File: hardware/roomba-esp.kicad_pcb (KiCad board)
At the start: 2 copper layers, 45 x 32.5 mm, 7 parts, among them P1 CONN_01X07, P2 CONN_02X10, U1 ESP-12E, U2 LM2596_module

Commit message: finalised rev0 pcb
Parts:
- P1: footprint mini din:mini din 7 -> mini din:mini_DIN_7
- moved U2 20.9 mm to (192.0, 118.0), turned to 0 degrees
- moved R1 13.4 mm to (181.0, 111.0), turned to 90 degrees
- moved D1 12.5 mm to (181.0, 116.0)
- moved R2 12.4 mm to (181.0, 121.0)
- moved P2 9.03 mm to (205.7, 127.0)
- moved P1 7.85 mm to (214.0, 98.5), turned to 90 degrees
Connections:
- P2 pad 10: /SCK -> /MISO
- P2 pad 12: /MOSI -> /CS0
- P2 pad 14: /MISO -> /GPIO16
- P2 pad 16: /CS0 -> /GPIO15
- P2 pad 18: /GPIO16 -> /GPIO14
- P2 pad 19: /GPIO14 -> /ADC
- P2 pad 20: /GPIO15 -> /RESET
- P2 pad 6: /ADC -> /SCK
- P2 pad 8: /RESET -> /MOSI
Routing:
- net /GPIO15: track 0.00 -> 52.3 mm, vias 0 -> 1
- net /RESET: track 0.00 -> 40.8 mm
- net /ADC: track 0.00 -> 36.4 mm
- net /GPIO13: track 16.2 -> 40.6 mm, vias 0 -> 1
- net /TX: track 0.00 -> 16.0 mm
- net /GPIO10: track 14.3 -> 29.6 mm, vias 1 -> 0
- net /SCK: track 15.3 -> 0.00 mm
- net /GPIO16: track 31.8 -> 44.0 mm
- net /GPIO14: track 21.5 -> 33.7 mm, vias 0 -> 1
- net /GPIO12: track 19.5 -> 28.5 mm, vias 0 -> 1
- net Net-(R1-Pad2): track 7.40 -> 15.8 mm
- net /MISO: track 14.0 -> 22.4 mm
- net /CS0: track 14.3 -> 22.2 mm
- net /RX: track 0.00 -> 7.36 mm
- net /DD: track 0.00 -> 7.20 mm
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- added copper zone on F.Cu, net GND
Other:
- board size 45 x 32.5 mm -> 33 x 40 mm
- net class Power: clearance 0.3 -> 0.25

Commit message: fixed some kicad-level path/library setings
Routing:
- net GND: track 4.62 -> 106.4 mm, vias 0 -> 1
- net VCC: track 7.48 -> 37.8 mm
- net /VBat: track 68.9 -> 39.5 mm
- net /SCK: track 0.00 -> 20.8 mm
- net /RESET: track 40.8 -> 45.1 mm, vias 0 -> 1
- net /GPIO0: track 30.2 -> 28.6 mm
- net /GPIO2: track 29.7 -> 29.9 mm, vias 0 -> 1
- added copper zone on B.Cu, net GND

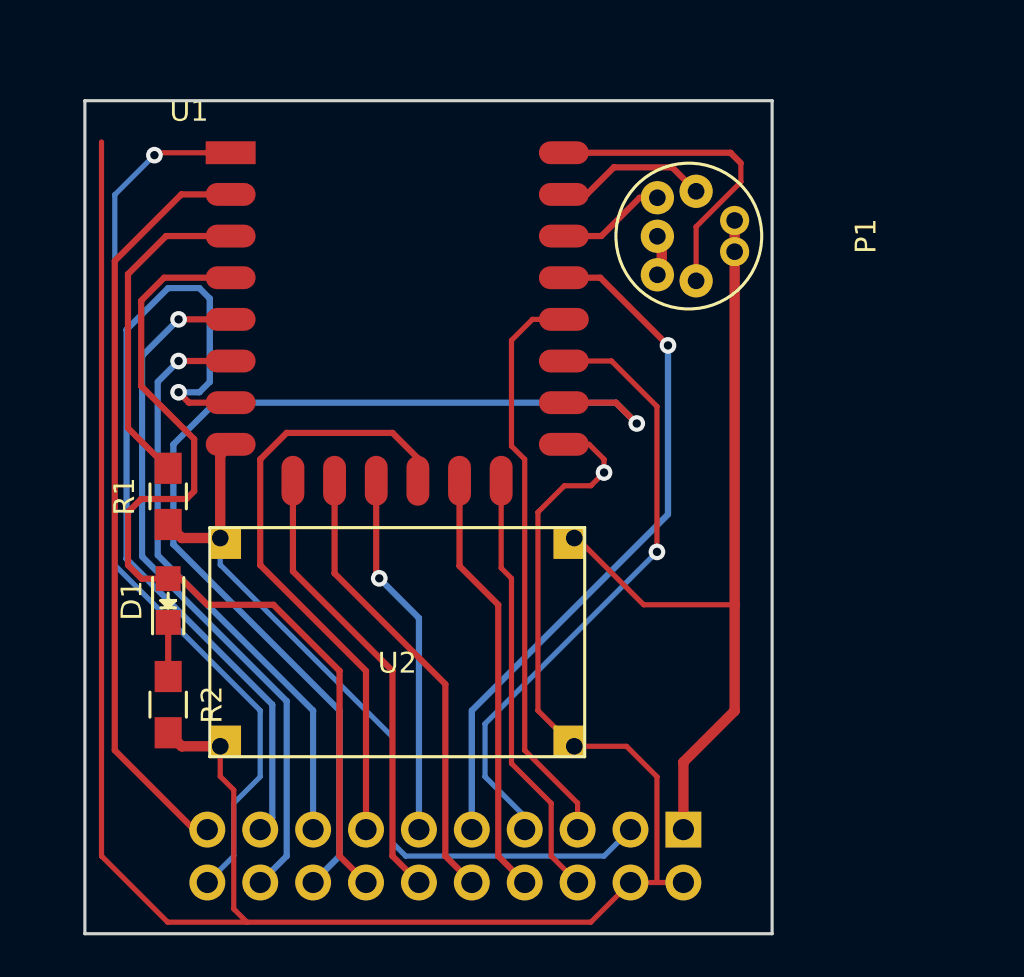
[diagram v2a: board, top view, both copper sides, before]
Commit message: added voltage divider on ESP RX to accomodate for 5V level on 3.3V pin
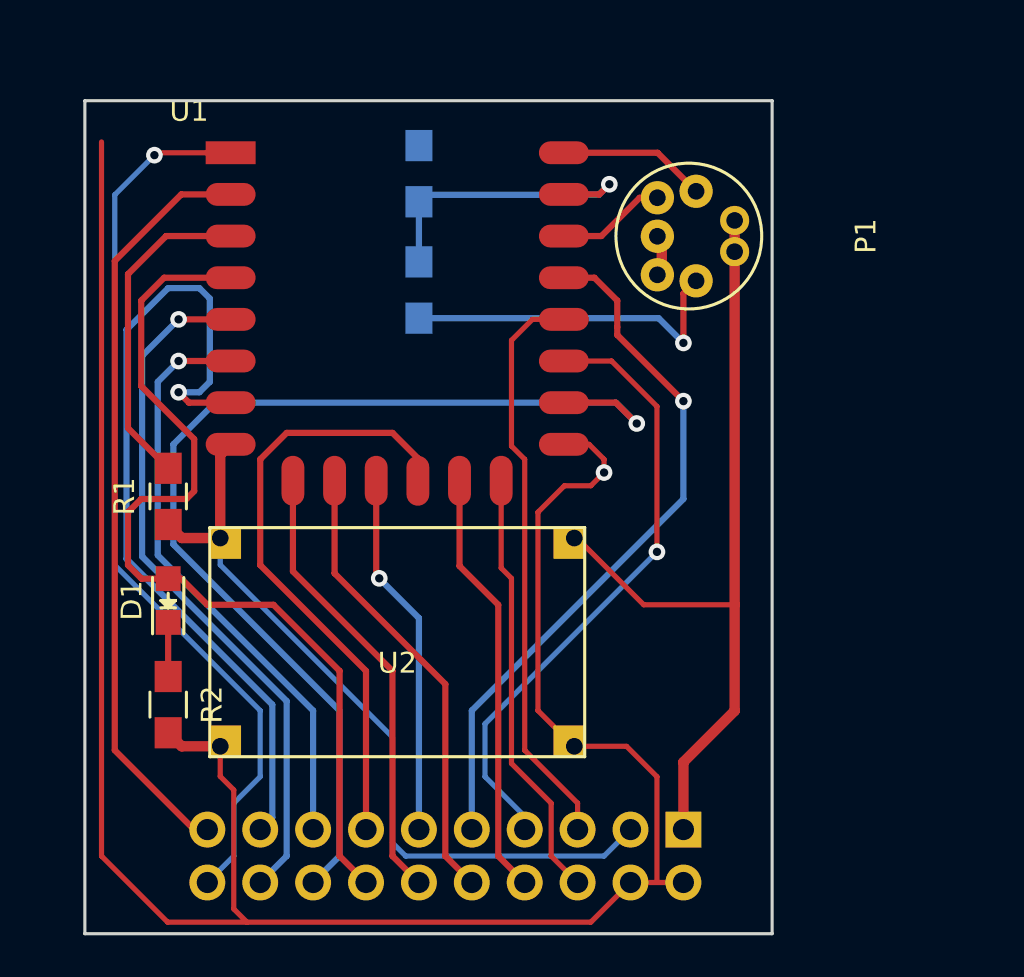
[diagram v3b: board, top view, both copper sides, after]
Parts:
- added R3: R, Resistors_SMD:R_0805_HandSoldering, B.Cu at (193.0, 101.1)
- added R4: R, Resistors_SMD:R_0805_HandSoldering, B.Cu at (193.0, 95.5)
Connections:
- P1 pad 3: /RX -> /RX_R
- P1 pad 4: /TX -> /TX_R
- U1 pad 22: /TX -> /RX_R
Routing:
- net /TX_R: track 0.00 -> 16.4 mm, vias 0 -> 1
- net /TX: track 16.0 -> 0.00 mm
- net /RX: track 7.36 -> 16.3 mm, vias 0 -> 1
- net /RX_R: track 0.00 -> 7.92 mm
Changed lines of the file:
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@@
-(kicad_pcb (version 4) (host pcbnew "(2015-09-21 BZR 6208, Git 1d27d08)-product")
+(kicad_pcb (version 4) (host pcbnew 0.201509251831+6217~30~ubuntu15.04.1-product)
   (general
-    (links 35)
+    (links 38)
     (no_connects 0)
-    (area 176.924999 91.924999 210.075001 132.075001)
+    (area 165.000001 85.773799 215.525 136.700001)
     (thickness 1.6)
     (drawings 6)
-    (tracks 192)
+    (tracks 202)
     (zones 0)
-    (modules 7)
-    (nets 25)
+    (modules 9)
+    (nets 26)
   )
   (page A4)
@@
     (31 B.Cu signal)
     (32 B.Adhes user)
-    (33 F.Adhes user)
+    (33 F.Adhes user hide)
     (34 B.Paste user)
     (35 F.Paste user)
@@
   )
   (setup
-    (last_trace_width 0.25)
+    (last_trace_width 0.3)
     (user_trace_width 0.25)
     (trace_clearance 0.25)
@@
   (net 22 /DD)
   (net 23 /RX)
-  (net 24 /TX)
+  (net 24 /TX_R)
+  (net 25 /RX_R)
   (net_class Default "This is the default net class."
     (clearance 0.25)
@@
     (add_net /RESET)
     (add_net /RX)
+    (add_net /RX_R)
     (add_net /SCK)
-    (add_net /TX)
+    (add_net /TX_R)
     (add_net "Net-(D1-Pad1)")
     (add_net "Net-(R1-Pad2)")
@@
       (net 23 /RX))
     (pad 22 smd oval (at 16 0) (size 2.4 1.1) (layers F.Cu F.Paste F.Mask)
-      (net 24 /TX))
+      (net 25 /RX_R))
   )
   (module Socket_Strips:Socket_Strip_Straight_2x10 (layer B.Cu)
@@
       (net 22 /DD))
     (pad 4 thru_hole circle (at -2.15 -7.65 90) (size 1.6 1.6) (drill 0.8) (layers *.Cu *.Mask F.SilkS)
-      (net 24 /TX))
+      (net 24 /TX_R))
     (pad 3 thru_hole circle (at 2.15 -7.65 90) (size 1.6 1.6) (drill 0.8) (layers *.Cu *.Mask F.SilkS)
-      (net 23 /RX))
+      (net 25 /RX_R))
     (pad 1 thru_hole circle (at 0.75 -5.8 90) (size 1.4 1.4) (drill 0.8) (layers *.Cu *.Mask F.SilkS)
       (net 3 /VBat))
     (pad 2 thru_hole circle (at -0.75 -5.8 90) (size 1.4 1.4) (drill 0.8) (layers *.Cu *.Mask F.SilkS)
       (net 3 /VBat))
+  )
+  (module Resistors_SMD:R_0805_HandSoldering (layer B.Cu)
+    (at 193.04 101.092 90)
+    (descr "Resistor SMD 0805, hand soldering")
+    (tags "resistor 0805")
+    (attr smd)
+    (fp_text reference R3 (at 0 2.1 90) (layer B.SilkS)
+      (effects (font (size 1 1) (thickness 0.15)) (justify mirror))
+    )
+    (fp_text value R (at 0 -2.1 90) (layer B.Fab)
+      (effects (font (size 1 1) (thickness 0.15)) (justify mirror))
+    )
+    (fp_line (start -2.4 1) (end 2.4 1) (layer B.CrtYd) (width 0.05))
+    (fp_line (start -2.4 -1) (end 2.4 -1) (layer B.CrtYd) (width 0.05))
+    (fp_line (start -2.4 1) (end -2.4 -1) (layer B.CrtYd) (width 0.05))
+    (fp_line (start 2.4 1) (end 2.4 -1) (layer B.CrtYd) (width 0.05))
+    (fp_line (start 0.6 -0.875) (end -0.6 -0.875) (layer B.SilkS) (width 0.15))
+    (fp_line (start -0.6 0.875) (end 0.6 0.875) (layer B.SilkS) (width 0.15))
+    (pad 1 smd rect (at -1.35 0 90) (size 1.5 1.3) (layers B.Cu B.Paste B.Mask)
+      (net 24 /TX_R))
+    (pad 2 smd rect (at 1.35 0 90) (size 1.5 1.3) (layers B.Cu B.Paste B.Mask)
+      (net 23 /RX))
+    (model Resistors_SMD.3dshapes/R_0805_HandSoldering.wrl
+      (at (xyz 0 0 0))
+      (scale (xyz 1 1 1))
+      (rotate (xyz 0 0 0))
+    )
+  )
+  (module Resistors_SMD:R_0805_HandSoldering (layer B.Cu)
+    (at 193.04 95.504 90)
+    (descr "Resistor SMD 0805, hand soldering")
+    (tags "resistor 0805")
+    (attr smd)
+    (fp_text reference R4 (at 0 2.1 90) (layer B.SilkS)
+      (effects (font (size 1 1) (thickness 0.15)) (justify mirror))
+    )
+    (fp_text value R (at 0 -2.1 90) (layer B.Fab)
+      (effects (font (size 1 1) (thickness 0.15)) (justify mirror))
+    )
+    (fp_line (start -2.4 1) (end 2.4 1) (layer B.CrtYd) (width 0.05))
+    (fp_line (start -2.4 -1) (end 2.4 -1) (layer B.CrtYd) (width 0.05))
+    (fp_line (start -2.4 1) (end -2.4 -1) (layer B.CrtYd) (width 0.05))
+    (fp_line (start 2.4 1) (end 2.4 -1) (layer B.CrtYd) (width 0.05))
+    (fp_line (start 0.6 -0.875) (end -0.6 -0.875) (layer B.SilkS) (width 0.15))
+    (fp_line (start -0.6 0.875) (end 0.6 0.875) (layer B.SilkS) (width 0.15))
+    (pad 1 smd rect (at -1.35 0 90) (size 1.5 1.3) (layers B.Cu B.Paste B.Mask)
+      (net 23 /RX))
+    (pad 2 smd rect (at 1.35 0 90) (size 1.5 1.3) (layers B.Cu B.Paste B.Mask)
+      (net 4 GND))
+    (model Resistors_SMD.3dshapes/R_0805_HandSoldering.wrl
+      (at (xyz 0 0 0))
+      (scale (xyz 1 1 1))
+      (rotate (xyz 0 0 0))
+    )
   )
   (dimension 40 (width 0.3) (layer Cmts.User)
@@
   (segment (start 182.88 129.54) (end 182.245 129.54) (width 0.3) (layer F.Cu) (net 9) (status 30))
   (segment (start 182.85218 94.5) (end 184 94.5) (width 0.3) (layer F.Cu) (net 9) (status 30))
-  (segment (start 195.58 127) (end 195.58 121.285) (width 0.3) (layer B.Cu) (net 10) (status 10))
-  (segment (start 201.75 100.5) (end 200 100.5) (width 0.3) (layer F.Cu) (net 10) (status 20))
-  (segment (start 205 103.75) (end 201.75 100.5) (width 0.3) (layer F.Cu) (net 10))
-  (via (at 205 103.75) (size 0.8) (drill 0.4) (layers F.Cu B.Cu) (net 10))
-  (segment (start 205 111.865) (end 205 103.75) (width 0.3) (layer B.Cu) (net 10))
-  (segment (start 195.58 121.285) (end 205 111.865) (width 0.3) (layer B.Cu) (net 10))
+  (segment (start 205.74 111.125) (end 205.74 106.426) (width 0.3) (layer B.Cu) (net 10))
+  (segment (start 201.465 100.5) (end 202.565 101.6) (width 0.3) (layer F.Cu) (net 10))
+  (segment (start 202.565 101.6) (end 202.565 102.87) (width 0.3) (layer F.Cu) (net 10))
+  (segment (start 195.58 121.285) (end 205.74 111.125) (width 0.3) (layer B.Cu) (net 10))
+  (segment (start 195.58 127) (end 195.58 121.285) (width 0.3) (layer B.Cu) (net 10))
+  (segment (start 201.465 100.5) (end 200 100.5) (width 0.3) (layer F.Cu) (net 10))
+  (segment (start 202.565 103.251) (end 202.565 102.87) (width 0.3) (layer F.Cu) (net 10))
+  (segment (start 205.74 106.426) (end 202.565 103.251) (width 0.3) (layer F.Cu) (net 10))
+  (via (at 205.74 106.426) (size 0.8) (drill 0.4) (layers F.Cu B.Cu) (net 10))
   (segment (start 200.66 129.54) (end 199.39 128.27) (width 0.25) (layer F.Cu) (net 11) (status 10))
   (segment (start 196.99 114.44) (end 196.99 110.25) (width 0.25) (layer F.Cu) (net 11) (status 20))
@@
   (segment (start 199.39 125.73) (end 197.485 123.825) (width 0.25) (layer F.Cu) (net 11))
   (segment (start 199.39 128.27) (end 199.39 125.73) (width 0.25) (layer F.Cu) (net 11))
+  (via (at 191.135 114.935) (size 0.8) (drill 0.4) (layers F.Cu B.Cu) (net 12))
   (segment (start 193.04 127) (end 193.04 116.84) (width 0.3) (layer B.Cu) (net 12) (status 10))
+  (segment (start 193.04 116.84) (end 191.135 114.935) (width 0.3) (layer B.Cu) (net 12))
   (segment (start 190.99 114.79) (end 190.99 110.25) (width 0.3) (layer F.Cu) (net 12) (status 20))
   (segment (start 191.135 114.935) (end 190.99 114.79) (width 0.3) (layer F.Cu) (net 12))
-  (via (at 191.135 114.935) (size 0.8) (drill 0.4) (layers F.Cu B.Cu) (net 12))
-  (segment (start 193.04 116.84) (end 191.135 114.935) (width 0.3) (layer B.Cu) (net 12))
   (segment (start 198.12 129.54) (end 196.85 128.27) (width 0.3) (layer F.Cu) (net 13) (status 10))
   (segment (start 194.99 114.345) (end 194.99 110.25) (width 0.3) (layer F.Cu) (net 13) (status 20))
@@
   (segment (start 200.3 98.5) (end 200 98.5) (width 0.3) (layer F.Cu) (net 22) (status 30))
   (segment (start 200 98.5) (end 201.1 98.5) (width 0.3) (layer F.Cu) (net 22) (status 30))
+  (segment (start 200 96.5) (end 201.696 96.5) (width 0.3) (layer F.Cu) (net 23))
+  (segment (start 201.676 96.52) (end 193.374 96.52) (width 0.3) (layer B.Cu) (net 23))
+  (segment (start 202.184 96.012) (end 201.676 96.52) (width 0.3) (layer B.Cu) (net 23))
+  (via (at 202.184 96.012) (size 0.8) (drill 0.4) (layers F.Cu B.Cu) (net 23))
+  (segment (start 201.696 96.5) (end 202.184 96.012) (width 0.3) (layer F.Cu) (net 23))
+  (segment (start 193.374 96.52) (end 193.04 96.854) (width 0.3) (layer B.Cu) (net 23))
+  (segment (start 193.374 96.52) (end 193.04 96.854) (width 0.3) (layer B.Cu) (net 23))
+  (segment (start 193.04 96.854) (end 193.04 99.742) (width 0.3) (layer B.Cu) (net 23))
   (segment (start 200 96.5) (end 201.1 96.5) (width 0.3) (layer F.Cu) (net 23) (status 30))
-  (segment (start 201.1 96.5) (end 202.4 95.2) (width 0.3) (layer F.Cu) (net 23) (status 10))
-  (segment (start 202.4 95.2) (end 205.2 95.2) (width 0.3) (layer F.Cu) (net 23))
-  (segment (start 205.2 95.2) (end 206.35 96.35) (width 0.3) (layer F.Cu) (net 23) (status 20))
-  (segment (start 200 94.5) (end 208 94.5) (width 0.3) (layer F.Cu) (net 24) (status 10))
-  (segment (start 206.35 98.05) (end 206.35 100.65) (width 0.25) (layer F.Cu) (net 24) (status 20))
-  (segment (start 208.5 95.9) (end 206.35 98.05) (width 0.25) (layer F.Cu) (net 24))
-  (segment (start 208.5 95) (end 208.5 95.9) (width 0.25) (layer F.Cu) (net 24))
-  (segment (start 208 94.5) (end 208.5 95) (width 0.3) (layer F.Cu) (net 24))
-  (segment (start 200.8 94.5) (end 200 94.5) (width 0.3) (layer F.Cu) (net 24) (status 30))
+  (segment (start 193.04 102.442) (end 204.55 102.442) (width 0.3) (layer B.Cu) (net 24))
+  (segment (start 205.74 101.26) (end 206.35 100.65) (width 0.3) (layer F.Cu) (net 24))
+  (segment (start 205.74 103.632) (end 205.74 101.26) (width 0.3) (layer F.Cu) (net 24))
+  (via (at 205.74 103.632) (size 0.8) (drill 0.4) (layers F.Cu B.Cu) (net 24))
+  (segment (start 204.55 102.442) (end 205.74 103.632) (width 0.3) (layer B.Cu) (net 24))
+  (segment (start 206.35 96.35) (end 204.5 94.5) (width 0.3) (layer F.Cu) (net 25))
+  (segment (start 204.5 94.5) (end 200 94.5) (width 0.3) (layer F.Cu) (net 25))
+  (segment (start 200.8 94.5) (end 200 94.5) (width 0.3) (layer F.Cu) (net 25) (status 30))
   (zone (net 4) (net_name GND) (layer F.Cu) (hatch edge 0.508)
     (connect_pads (clearance 0.508))

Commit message: rearrenged roomba connector and voltage divider
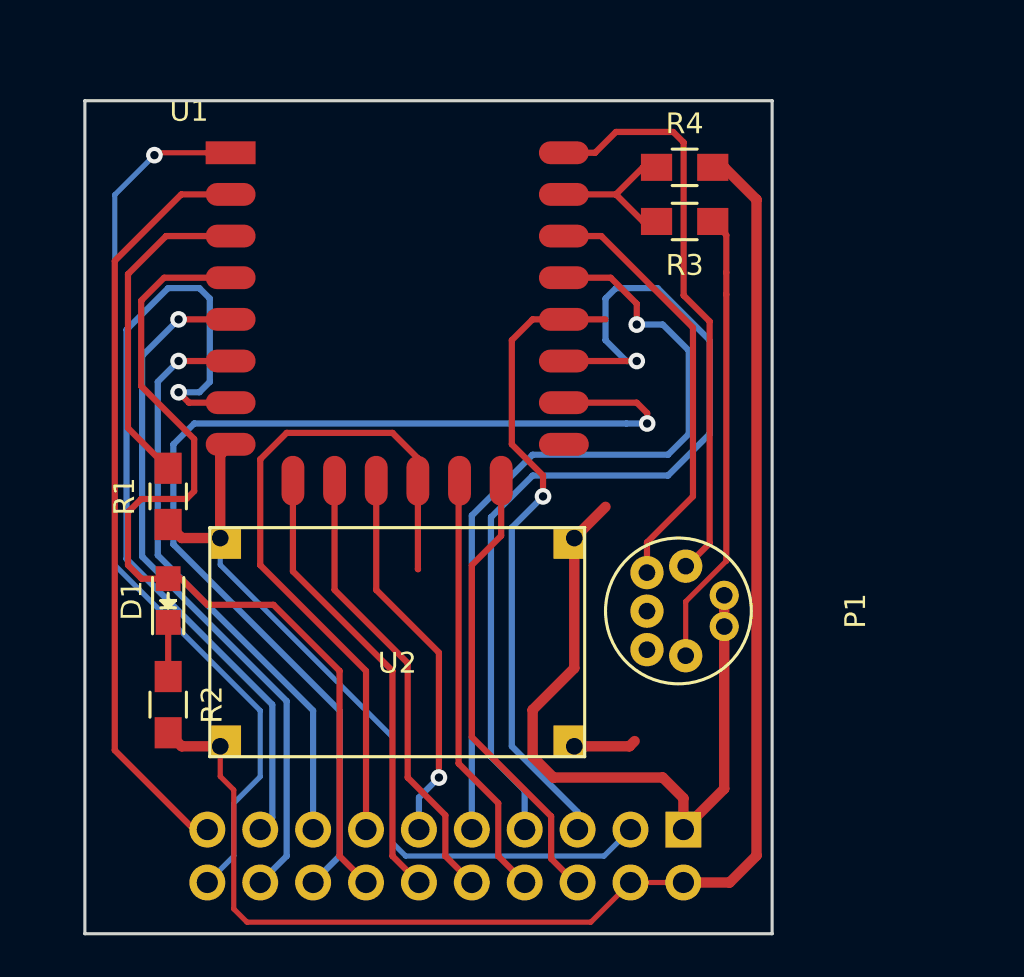
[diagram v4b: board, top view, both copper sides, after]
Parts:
- R3, R4: moved to F.Cu
- moved P1 18.0 mm to (213.5, 116.5)
- moved R3 13.2 mm to (205.8, 97.8), turned to 180 degrees
- moved R4 12.8 mm to (205.8, 95.2), turned to 0 degrees
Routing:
- net GND: track 106.4 -> 74.8 mm, vias 1 -> 0
- net /RX_R: track 7.92 -> 28.5 mm
- net /GPIO2: track 29.9 -> 46.6 mm
- net /DD: track 7.20 -> 22.1 mm
- net /RX: track 16.3 -> 8.58 mm, vias 1 -> 0
- net /TX_R: track 16.4 -> 21.9 mm, vias 1 -> 0
- net /GPIO5: track 33.9 -> 39.2 mm
- net /GPIO10: track 29.6 -> 33.8 mm
- net /VBat: track 39.5 -> 35.2 mm
- net /GPIO0: track 28.6 -> 31.8 mm, vias 0 -> 1
- net /SCK: track 20.8 -> 22.1 mm
- net /GPIO9: track 17.6 -> 18.4 mm

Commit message: added serial header to pcb
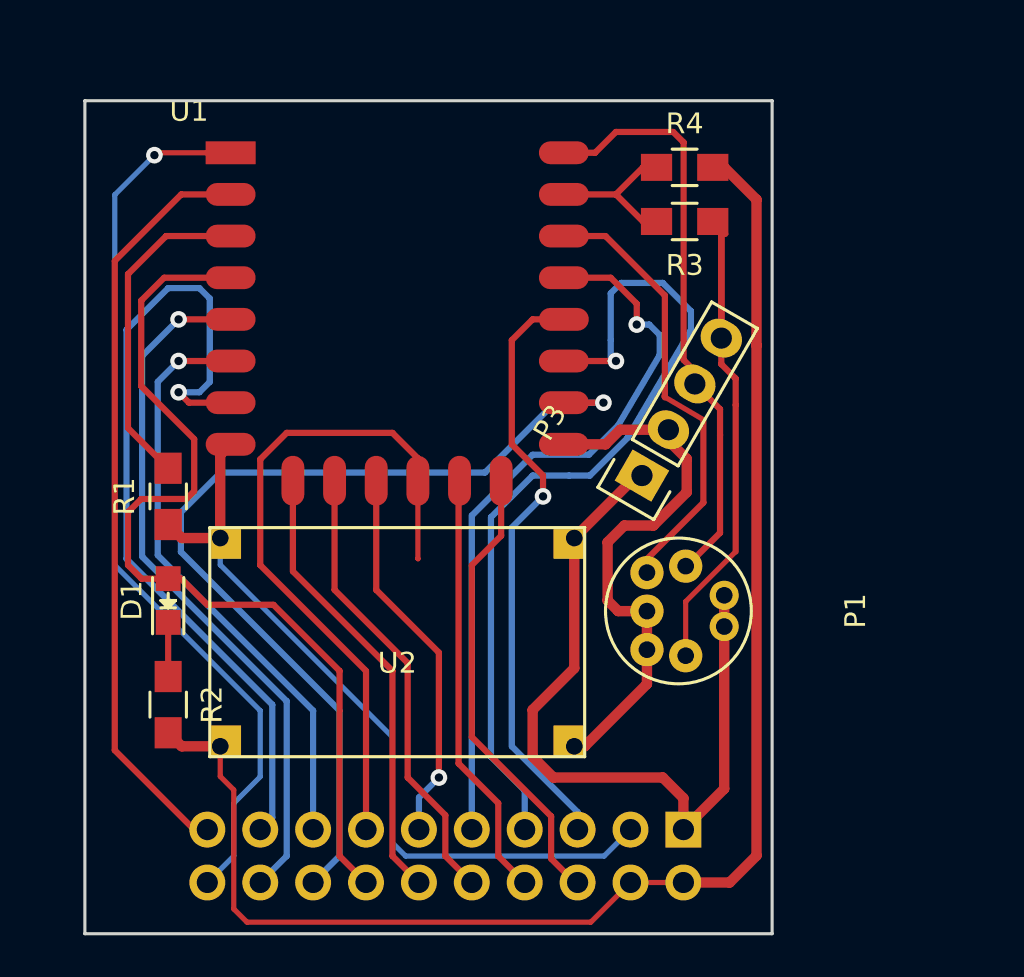
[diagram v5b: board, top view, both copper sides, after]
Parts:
- added P3: CONN_01X04, Socket_Strips:Socket_Strip_Straight_1x04, F.Cu at (203.8, 110.0)
- P2: footprint Socket_Strips:Socket_Strip_Straight_2x10 -> Socket_Strips:Socket_Strip_Angled_2x10
- R3: value R -> 5K
- R4: value R -> 10K
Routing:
- net GND: track 74.8 -> 98.4 mm
- net /TX_R: track 21.9 -> 28.9 mm
- net /GPIO15: track 52.7 -> 45.8 mm
- net /GPIO2: track 46.6 -> 42.0 mm
- net /GPIO5: track 39.2 -> 35.1 mm
- net /VBat: track 35.2 -> 37.8 mm
- net /GPIO0: track 31.8 -> 29.8 mm
- net /DD: track 22.1 -> 22.9 mm
- net /GPIO10: track 33.8 -> 33.3 mm
